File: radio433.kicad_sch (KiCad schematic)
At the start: 31 parts, among them J1 TX, J2 RX, U1 MICRF113YM6-TR, U2 MICRF219AAYQS, Y2 13M52313, Y3 13M56

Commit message: changed shape
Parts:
- C6: value 100p -> 100p(100n)
- R1: value 100k -> 100k(22k)
- R3: value 50k -> 50k(10k)
- Y2: value 13M52313 -> 13M52313(13M56)
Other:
- note added: "concept(finally placed)"
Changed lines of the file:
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@@
 		)
 	)
+	(text "concept(finally placed)"
+		(exclude_from_sim no)
+		(at 45.974 145.796 0)
+		(effects
+			(font
+				(size 1.27 1.27)
+			)
+		)
+	)
 	(label "ANT"
 		(at 205.74 60.96 0)
@@
 			)
 		)
-		(property "Value" "13M52313"
+		(property "Value" "13M52313(13M56)"
 			(at 186.69 53.594 90)
 			(effects
@@
 			)
 		)
-		(property "Value" "50k"
-			(at 195.58 73.914 0)
+		(property "Value" "50k(10k)"
+			(at 192.024 76.2 0)
 			(effects
 				(font
@@
 			)
 		)
-		(property "Value" "100p"
-			(at 83.82 120.65 0)
+		(property "Value" "100p(100n)"
+			(at 76.454 120.904 0)
 			(effects
 				(font
@@
 			)
 		)
-		(property "Value" "100k"
-			(at 52.07 142.24 0)
+		(property "Value" "100k(22k)"
+			(at 46.99 142.748 0)
 			(effects
 				(font

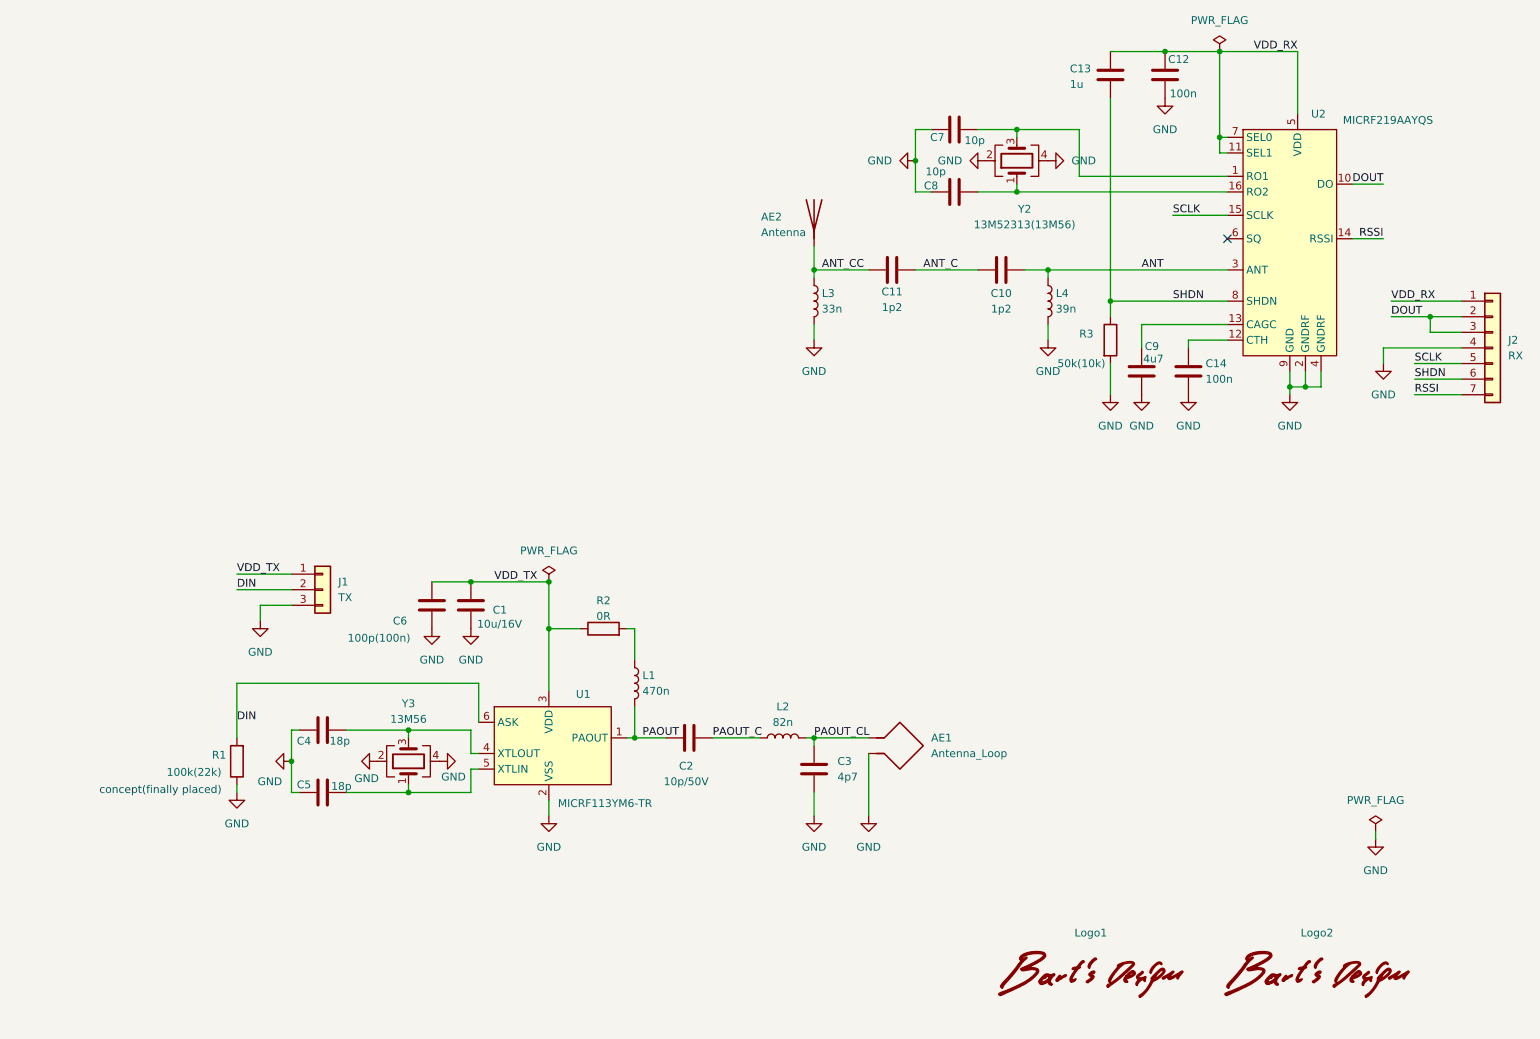
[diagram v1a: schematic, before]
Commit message: remover receiver
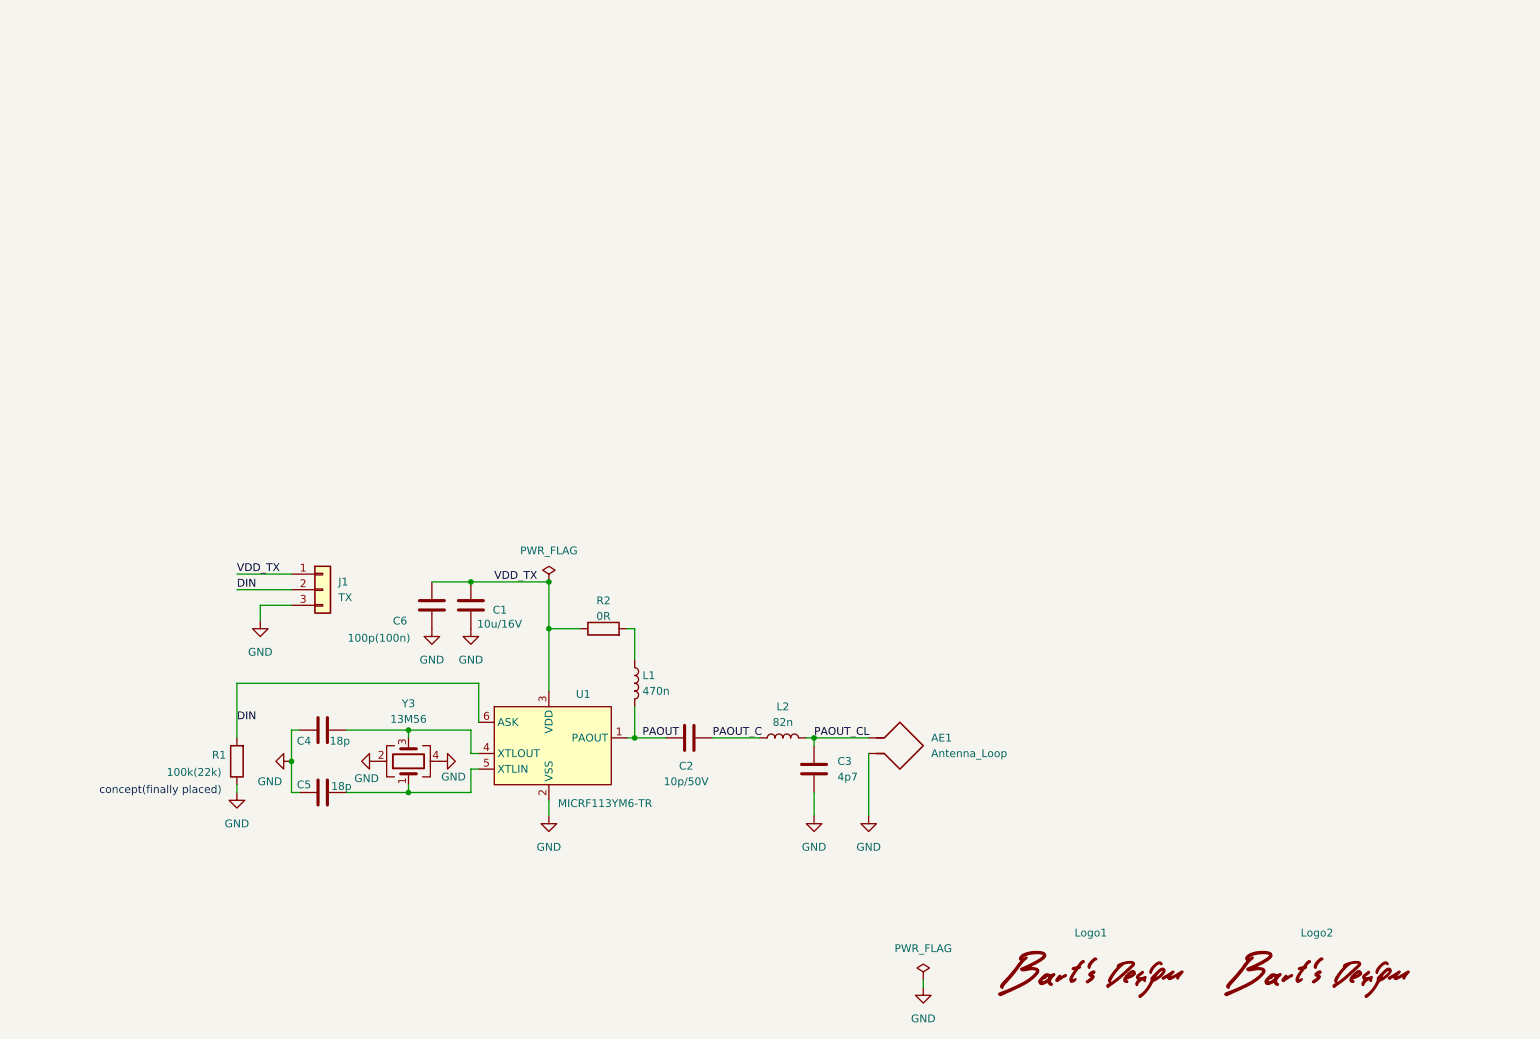
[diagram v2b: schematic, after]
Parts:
- removed AE2: Antenna, radio433Lib:antenna_433_50R_helical, symbol Device:Antenna
- removed C10, C11: 1p2, Capacitor_SMD:C_0603_1608Metric, symbol Device:C
- removed C12, C14: 100n, Capacitor_SMD:C_0603_1608Metric, symbol Device:C
- removed C13: 1u, Capacitor_SMD:C_0603_1608Metric, symbol Device:C
- removed C7, C8: 10p, Capacitor_SMD:C_0603_1608Metric, symbol Device:C
- removed C9: 4u7, Capacitor_SMD:C_0805_2012Metric, symbol Device:C
- removed J2: RX, Connector_PinHeader_2.54mm:PinHeader_1x07_P2.54mm_Vertical, symbol Connector_Generic:Conn_01x07
- removed L3: 33n, Inductor_SMD:L_0603_1608Metric, symbol Device:L
- removed L4: 39n, Inductor_SMD:L_0603_1608Metric, symbol Device:L
- removed R3: 50k(10k), Inductor_SMD:L_0603_1608Metric, symbol Device:R
- removed U2: MICRF219AAYQS, Package_SO:QSOP-16_3.9x4.9mm_P0.635mm, symbol radio433Lib:MICRF219AAYQS
- removed Y2: 13M52313(13M56), Crystal:Crystal_SMD_3225-4Pin_3.2x2.5mm, symbol Device:Crystal_GND24
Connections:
- no-connect marks 1 -> 0

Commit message: V3
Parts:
- added AE3: Antenna_Shield, Connector_PinSocket_2.54mm:PinSocket_1x02_P2.54mm_Vertical, symbol Device:Antenna_Shield
- added C10: 2p7, Capacitor_SMD:C_0603_1608Metric, symbol Device:C
- added C11: 6p2, Capacitor_SMD:C_0603_1608Metric, symbol Device:C
- added C7: 1n, Capacitor_SMD:C_0603_1608Metric, symbol Device:C
- added C8: 100nF, Capacitor_SMD:C_0805_2012Metric, symbol Device:C
- added C9: NC, Capacitor_SMD:C_0603_1608Metric, symbol Device:C
- added J2: RX, Connector_PinHeader_2.54mm:PinHeader_1x05_P2.54mm_Vertical, symbol Connector_Generic:Conn_01x05
- added L3: 33nH, Inductor_SMD:L_0603_1608Metric, symbol Device:L
- added L4: 22nH, Inductor_SMD:L_0603_1608Metric, symbol Device:L
- added R3: 10k, Resistor_SMD:R_0603_1608Metric, symbol Device:R
- added U2: CMT2210LC, Package_SO:SO-8_3.9x4.9mm_P1.27mm, symbol radio433Lib:CMT2210LC
- added Y2: 27M1383, Crystal:Crystal_SMD_3225-4Pin_3.2x2.5mm, symbol Device:Crystal_GND24
- Y3: Field5 (none) -> 3225-13.56M-SR
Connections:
- net GND: now also AE3.2 (Shield), C11.2, C7.2, C8.1, C9.2, J2.5 (Pin_5), L3.2, L4.2, R3.1, U2.1 (GND), Y2.1, Y2.2, Y2.4
- net VDD_TX renamed VDD
- net VDD: now also C7.1, C8.2, J2.2 (Pin_2), U2.2 (VDD)
- new net: AE3.1 (A), C10.1, C11.1, L4.1
- new net: C10.2, C9.1, L3.1, U2.8 (RFIN)
- new net: U2.5 (XIN), Y2.3
- new net DOUT: J2.3 (Pin_3), J2.4 (Pin_4), U2.3 (DOUT)
- new net SHDN: J2.1 (Pin_1), R3.2, U2.4 (SDN)
